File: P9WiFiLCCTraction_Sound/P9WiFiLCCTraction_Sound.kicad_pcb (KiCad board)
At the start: 2 copper layers, 103.5 x 22.9 mm, 31 parts, among them IC102 MP6614GN-Z, J101 USB_C_Receptacle, J102 DCC 9-pin, SW101 Reset, SW102 Boot, U101 ESP32_S3_WROOM, U102 TBD62064AFG_1, U103 AP63203WU

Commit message: Complete P9WiFiLCCTraction_Sound hardware.
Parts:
- added C111: .1uf, Capacitor_SMD:C_0402_1005Metric, F.Cu at (162.1, 105.6)
- added C112: 10uf 6.3V, Capacitor_SMD:C_0603_1608Metric, F.Cu at (162.2, 101.0)
- added R104: 0, Resistor_SMD:R_0402_1005Metric, F.Cu at (164.2, 101.6)
- added TP101: Speaker, TestPoint:TestPoint_2Pads_Pitch2.54mm_Drill0.8mm, F.Cu at (163.1, 108.2)
- added U104: MAX98357AETE+T, Package_DFN_QFN:TQFN-16-1EP_3x3mm_P0.5mm_EP1.23x1.23mm_ThermalVias, F.Cu at (164.9, 104.8)
- moved C104 5.80 mm to (156.2, 104.3)
- moved C103 5.80 mm to (156.3, 101.3)
- moved C105 5.74 mm to (159.3, 103.1)
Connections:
- U101 pad 19: unconnected-(U101-Pad19) -> /I2S_TX
- U101 pad 20: unconnected-(U101-Pad20) -> /I2S_BCLK
- U101 pad 21: unconnected-(U101-Pad21) -> /LRCLK
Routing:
- net GND: track 89.7 -> 104.6 mm
- net /Function3: track 83.2 -> 93.3 mm, vias 2 -> 4
- net /Function4: track 88.0 -> 97.6 mm, vias 2 -> 4
- net /Function2: track 88.9 -> 94.1 mm, vias 4 -> 6
- net /I2S_TX: track 0.00 -> 3.11 mm
- net /MForward: track 83.8 -> 86.7 mm
- net /MReverse: track 82.1 -> 84.8 mm
- net Net-(TP101-Pad1): track 0.00 -> 2.35 mm
- net Net-(TP101-Pad2): track 0.00 -> 2.31 mm
- net /I2S_BCLK: track 0.00 -> 2.18 mm
- net /LRCLK: track 0.00 -> 2.11 mm
- net Net-(R104-Pad2): track 0.00 -> 1.25 mm
- net /Function1: track 88.8 -> 89.3 mm
- net +3V3: track 29.0 -> 29.5 mm

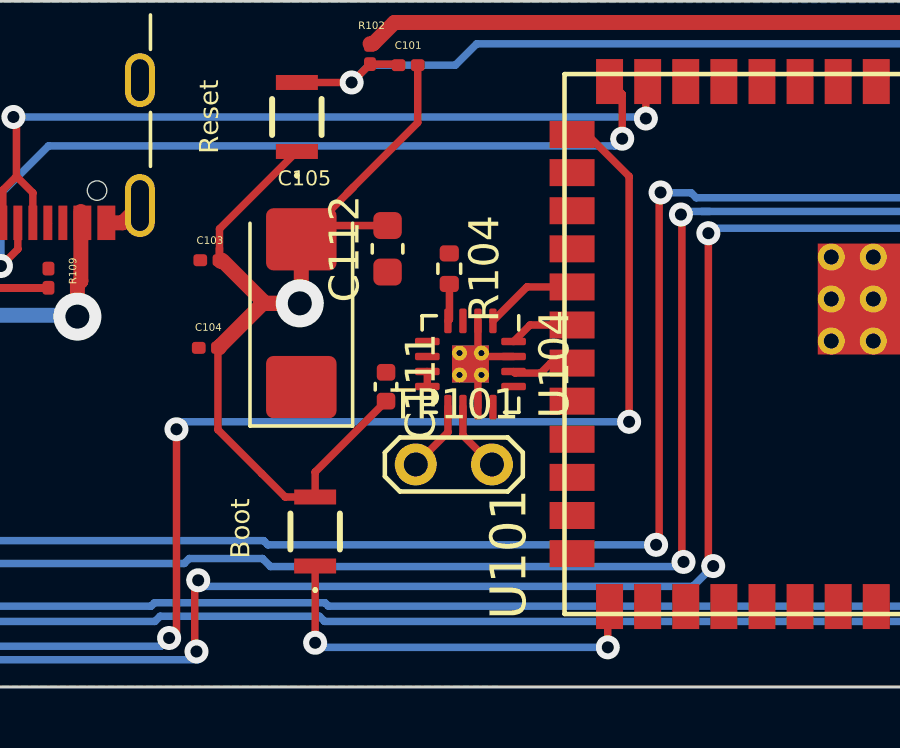
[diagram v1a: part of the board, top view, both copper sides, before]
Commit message: Final (silkscreen) tweaks, Image files generated.
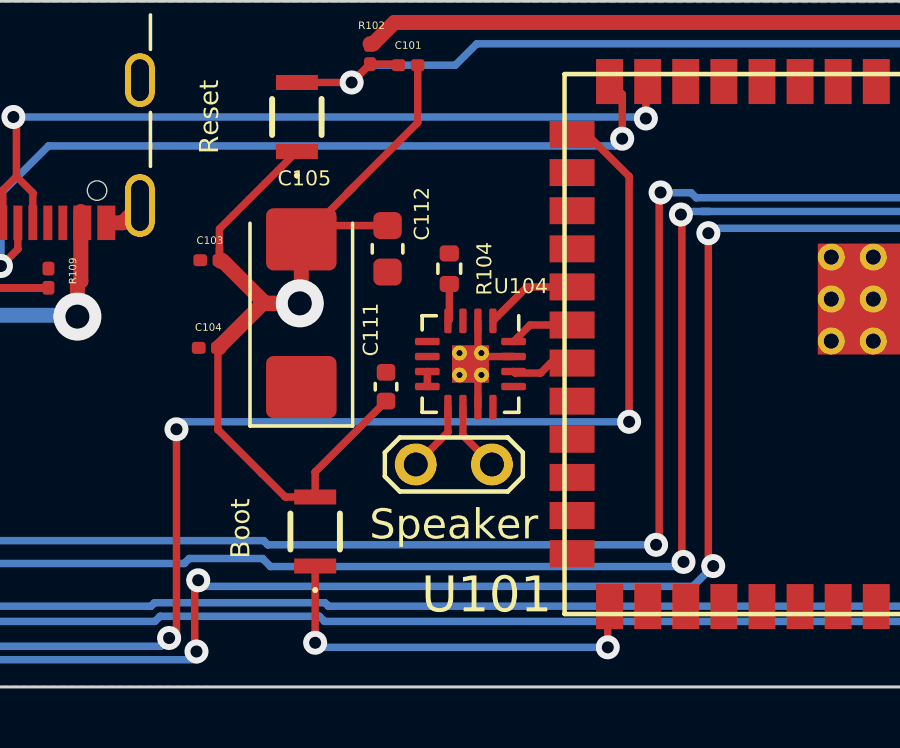
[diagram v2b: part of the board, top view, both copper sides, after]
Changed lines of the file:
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@@
     (property "Sheetname" "")
     (attr smd)
-    (fp_text reference "C112" (at 0 -1.43 90) (layer "F.SilkS")
-      (effects (font (size 1 1) (thickness 0.15)))
+    (fp_text reference "C112" (at 1.1684 1.143 90) (layer "F.SilkS")
+      (effects (font (size 0.5 0.5) (thickness 0.075)))
     )
     (fp_text value "10uf 6.3V" (at 0 1.43 90) (layer "F.Fab")
@@
     (property "Value_1" "MAX98357AETE+T")
     (attr smd)
-    (fp_text reference "U104" (at 0 -2.8 -90) (layer "F.SilkS")
-      (effects (font (size 1 1) (thickness 0.15)))
+    (fp_text reference "U104" (at -2.596 -1.6816) (layer "F.SilkS")
+      (effects (font (size 0.5 0.5) (thickness 0.075)))
     )
     (fp_text value "MAX98357AETE+T" (at 0 2.8 -90) (layer "F.Fab")
@@
     (pad "17" thru_hole circle (at -0.365 -0.365 270) (size 0.5 0.5) (drill 0.2) (layers *.Cu)
       (net 2 "GND") (pinfunction "THERMAL_PAD") (pintype "passive"))
-    (model "${KICAD6_3DMODEL_DIR}/Package_DFN_QFN.3dshapes/TQFN-16-1EP_3x3mm_P0.5mm_EP1.23x1.23mm.wrl"
+    (model "${KICAD6_3DMODEL_DIR}/Package_DFN_QFN.3dshapes/QFN-16-1EP_3x3mm_P0.5mm_EP1.8x1.8mm.wrl"
       (offset (xyz 0 0 0))
       (scale (xyz 1 1 1))
@@
     (attr smd)
     (fp_text reference "R104" (at 0 -1.17 90) (layer "F.SilkS")
-      (effects (font (size 1 1) (thickness 0.15)))
+      (effects (font (size 0.5 0.5) (thickness 0.075)))
     )
     (fp_text value "0" (at 0 1.17 90) (layer "F.Fab")
@@
     (property "Sheetname" "")
     (attr exclude_from_pos_files)
-    (fp_text reference "TP101" (at 1.3 -2) (layer "F.SilkS")
-      (effects (font (size 1 1) (thickness 0.15)))
-    )
-    (fp_text value "Speaker" (at 1.27 2) (layer "F.Fab")
+    (fp_text reference "TP101" (at 1.3 -2) (layer "F.Fab")
+      (effects (font (size 1 1) (thickness 0.15)))
+    )
+    (fp_text value "Speaker" (at 1.27 2) (layer "F.SilkS")
       (effects (font (size 1 1) (thickness 0.15)))
     )
@@
     (property "Sheetname" "")
     (attr through_hole)
-    (fp_text reference "U101" (at 7.0104 10.9819 -90) (layer "F.SilkS")
+    (fp_text reference "U101" (at 8.3566 11.7185) (layer "F.SilkS")
       (effects (font (size 1.2 1.2) (thickness 0.15)))
     )
@@
     (property "Sheetname" "")
     (attr smd)
-    (fp_text reference "C111" (at 0 -1.16 90) (layer "F.SilkS")
-      (effects (font (size 1 1) (thickness 0.15)))
+    (fp_text reference "C111" (at -1.905 0.508 90) (layer "F.SilkS")
+      (effects (font (size 0.5 0.5) (thickness 0.075)))
     )
     (fp_text value ".1uf" (at 0 1.16 90) (layer "F.Fab")
